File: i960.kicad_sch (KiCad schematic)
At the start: 49 parts

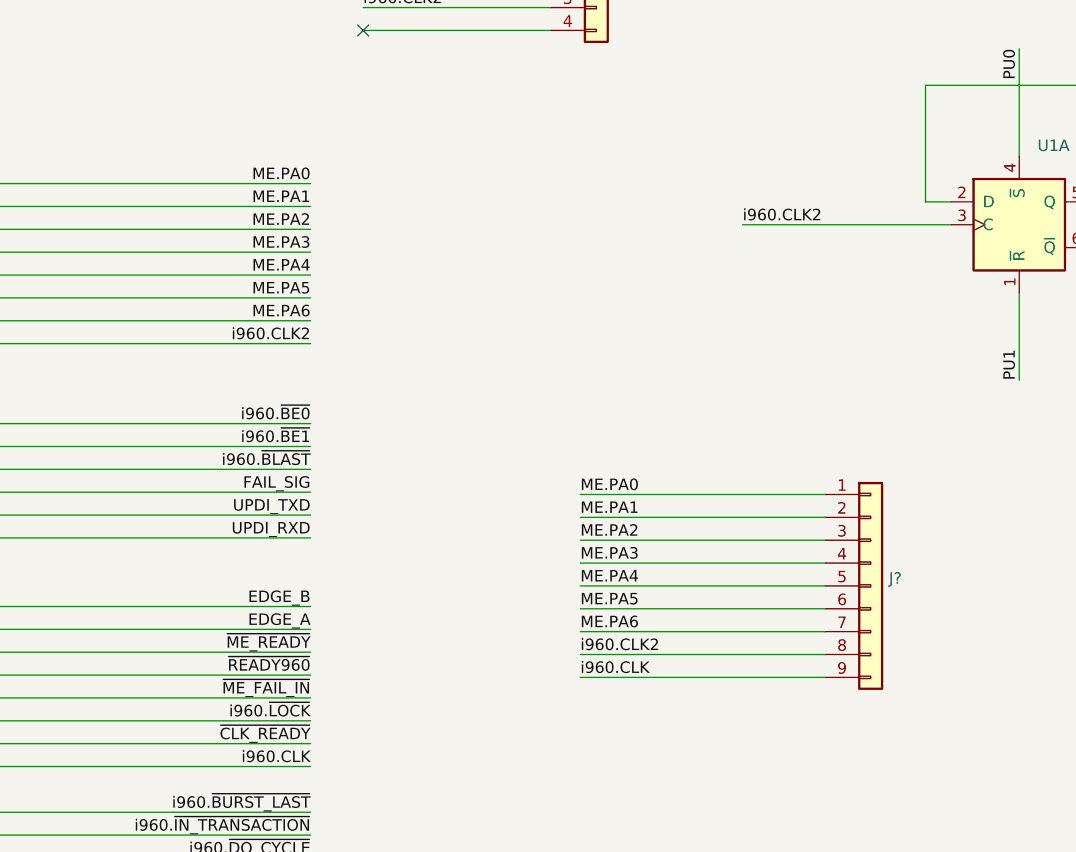
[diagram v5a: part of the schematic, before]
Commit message: Drop the HC125 and start redoing the pinout for the management engine to maximize layout capabilities
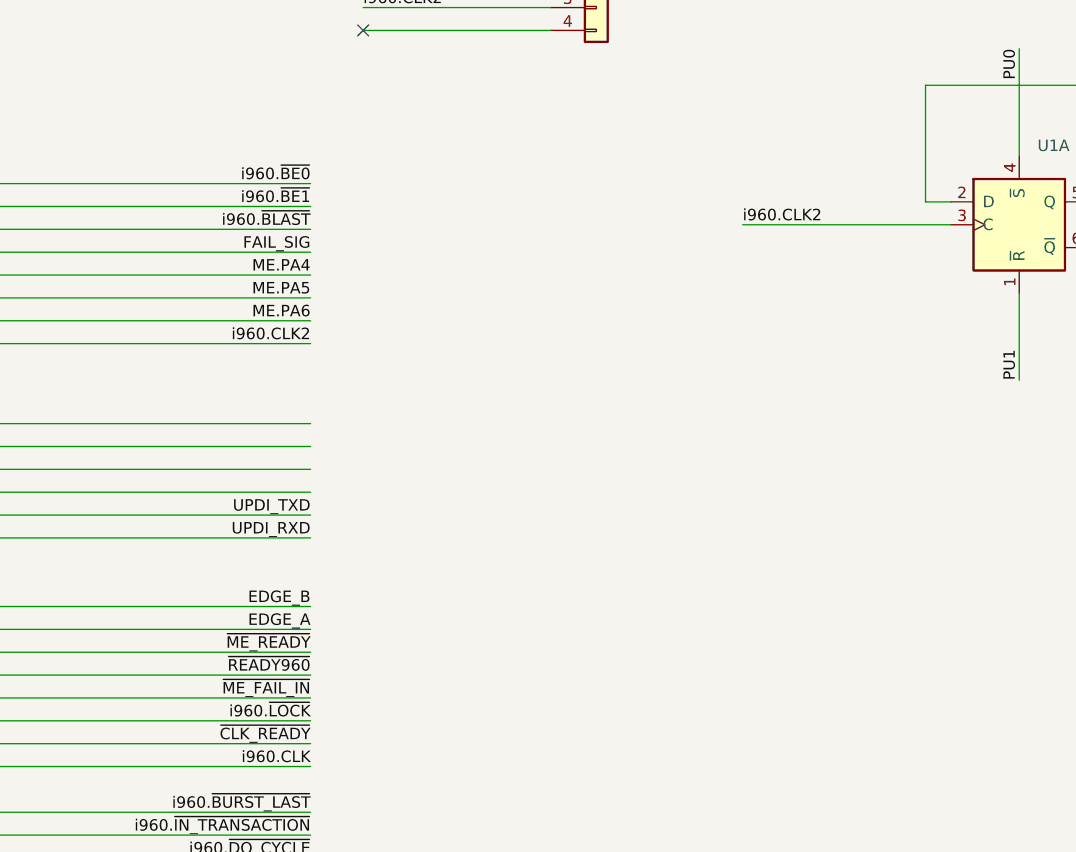
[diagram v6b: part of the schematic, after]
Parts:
- removed J?: (no value), symbol Connector_Generic:Conn_01x09
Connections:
- net ME.PA0 is gone; now on net i960.~{BE0}: U16.33 ((CLKI/TXD0/CCL0-IN0)PA0)
- net ME.PA1 is gone; now on net i960.~{BE1}: U16.34 ((RXD0/CCL0-IN1)PA1)
- net ME.PA2 is gone; now on net i960.~{BLAST}: U16.35 ((XCK0/SDA/CCL0-IN2)PA2)
- net ME.PA3 is gone; now on net FAIL_SIG: U16.36 ((XDIR0/SCL/CCL0-OUT)PA3)
- net FAIL_SIG: no longer U16.4 ((XDIR1/~{SS}_ALT/CCL1-OUT)PC3)
- net i960.~{BE0}: no longer U16.1 ((TXD1/MOSI_ALT/CCL1-IN0)PC0)
- net i960.~{BE1}: no longer U16.2 ((RXD1/MISO_ALT/CCL1-IN1)PC1)
- net i960.~{BLAST}: no longer U16.3 ((XCK1/SCK_ALT/CCL1-IN2)PC2)
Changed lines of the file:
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@@
-    (stroke (width 0) (type default) (color 0 0 0 0))
-  )
-  (wire (pts (xy 172.466 84.582) (xy 199.644 84.582))
     (stroke (width 0) (type default) (color 0 0 0 0))
   )
@@
     (stroke (width 0) (type default) (color 0 0 0 0))
   )
-  (wire (pts (xy 172.466 76.962) (xy 199.644 76.962))
-    (stroke (width 0) (type default) (color 0 0 0 0))
-  )
   (wire (pts (xy 514.604 80.264) (xy 542.29 80.264))
     (stroke (width 0) (type default) (color 0 0 0 0))
@@
     (stroke (width 0) (type default) (color 0 0 0 0))
   )
-  (wire (pts (xy 172.466 89.662) (xy 199.644 89.662))
-    (stroke (width 0) (type default) (color 0 0 0 0))
-  )
   (wire (pts (xy 45.212 135.128) (xy 45.212 118.11))
     (stroke (width 0) (type default) (color 0 0 0 0))
@@
     (stroke (width 0) (type default) (color 0 0 0 0))
   )
-  (wire (pts (xy 172.466 79.502) (xy 199.644 79.502))
-    (stroke (width 0) (type default) (color 0 0 0 0))
-  )
   (wire (pts (xy 210.312 462.788) (xy 210.312 427.736))
     (stroke (width 0) (type default) (color 0 0 0 0))
@@
     (stroke (width 0) (type default) (color 0 0 0 0))
   )
-  (wire (pts (xy 172.466 97.282) (xy 199.644 97.282))
-    (stroke (width 0) (type default) (color 0 0 0 0))
-  )
   (wire (pts (xy 59.69 61.468) (xy 20.066 61.468))
     (stroke (width 0) (type default) (color 0 0 0 0))
@@
     (stroke (width 0) (type default) (color 0 0 0 0))
   )
-  (wire (pts (xy 172.466 82.042) (xy 199.644 82.042))
-    (stroke (width 0) (type default) (color 0 0 0 0))
-  )
   (wire (pts (xy 23.876 364.236) (xy 54.102 364.236))
     (stroke (width 0) (type default) (color 0 0 0 0))
@@
     (stroke (width 0) (type default) (color 0 0 0 0))
   )
-  (wire (pts (xy 172.466 94.742) (xy 199.644 94.742))
-    (stroke (width 0) (type default) (color 0 0 0 0))
-  )
   (wire (pts (xy 467.106 57.404) (xy 502.92 57.404))
     (stroke (width 0) (type default) (color 0 0 0 0))
@@
     (stroke (width 0) (type default) (color 0 0 0 0))
   )
-  (wire (pts (xy 172.466 92.202) (xy 199.644 92.202))
-    (stroke (width 0) (type default) (color 0 0 0 0))
-  )
   (wire (pts (xy 346.71 266.446) (xy 377.698 266.446))
     (stroke (width 0) (type default) (color 0 0 0 0))
@@
   )
   (wire (pts (xy 148.336 25.4) (xy 169.164 25.4))
-    (stroke (width 0) (type default) (color 0 0 0 0))
-  )
-  (wire (pts (xy 172.466 87.122) (xy 199.644 87.122))
     (stroke (width 0) (type default) (color 0 0 0 0))
   )
@@
     (effects (font (size 1.27 1.27)) (justify left bottom))
   )
-  (label "FAIL_SIG" (at 142.494 76.708 180)
+  (label "FAIL_SIG" (at 142.494 50.038 180)
     (effects (font (size 1.27 1.27)) (justify right bottom))
   )
@@
     (effects (font (size 1.27 1.27)) (justify left bottom))
   )
-  (label "ME.PA4" (at 172.466 87.122 0)
-    (effects (font (size 1.27 1.27)) (justify left bottom))
-  )
   (label "~{RESET_INTERMEDIATE}" (at 142.494 132.588 180)
     (effects (font (size 1.27 1.27)) (justify right bottom))
@@
     (effects (font (size 1.27 1.27)) (justify right bottom))
   )
-  (label "ME.PA0" (at 172.466 76.962 0)
-    (effects (font (size 1.27 1.27)) (justify left bottom))
-  )
   (label "AD1" (at 405.892 44.704 0)
     (effects (font (size 1.27 1.27)) (justify left bottom))
@@
     (effects (font (size 1.27 1.27)) (justify left bottom))
   )
-  (label "ME.PA1" (at 172.466 79.502 0)
-    (effects (font (size 1.27 1.27)) (justify left bottom))
-  )
   (label "i960.D0" (at 489.966 170.942 0)
     (effects (font (size 1.27 1.27)) (justify left bottom))
@@
     (effects (font (size 1.27 1.27)) (justify left bottom))
   )
-  (label "i960.CLK2" (at 172.466 94.742 0)
-    (effects (font (size 1.27 1.27)) (justify left bottom))
-  )
   (label "PU3" (at 294.386 119.634 90)
     (effects (font (size 1.27 1.27)) (justify left bottom))
@@
     (effects (font (size 1.27 1.27)) (justify right bottom))
   )
-  (label "ME.PA2" (at 142.494 47.498 180)
-    (effects (font (size 1.27 1.27)) (justify right bottom))
-  )
   (label "PU0" (at 221.234 27.432 270)
     (effects (font (size 1.27 1.27)) (justify right bottom))
@@
     (effects (font (size 1.27 1.27)) (justify right bottom))
   )
-  (label "i960.~{BLAST}" (at 142.494 74.168 180)
+  (label "i960.~{BLAST}" (at 142.494 47.498 180)
     (effects (font (size 1.27 1.27)) (justify right bottom))
   )
@@
     (effects (font (size 1.27 1.27)) (justify right bottom))
   )
-  (label "ME.PA5" (at 172.466 89.662 0)
-    (effects (font (size 1.27 1.27)) (justify left bottom))
-  )
   (label "AD6" (at 405.892 57.404 0)
     (effects (font (size 1.27 1.27)) (justify left bottom))
@@
     (effects (font (size 1.27 1.27)) (justify left bottom))
   )
-  (label "ME.PA1" (at 142.494 44.958 180)
-    (effects (font (size 1.27 1.27)) (justify right bottom))
-  )
   (label "GCM4.L7" (at 477.52 191.516 180)
     (effects (font (size 1.27 1.27)) (justify right bottom))
@@
     (effects (font (size 1.27 1.27)) (justify left bottom))
   )
-  (label "ME.PA3" (at 142.494 50.038 180)
-    (effects (font (size 1.27 1.27)) (justify right bottom))
-  )
-  (label "i960.~{BE0}" (at 142.494 69.088 180)
+  (label "i960.~{BE0}" (at 142.494 42.418 180)
     (effects (font (size 1.27 1.27)) (justify right bottom))
   )
@@
     (effects (font (size 1.27 1.27)) (justify left bottom))
   )
-  (label "i960.~{BE1}" (at 142.494 71.628 180)
-    (effects (font (size 1.27 1.27)) (justify right bottom))
-  )
-  (label "ME.PA3" (at 172.466 84.582 0)
-    (effects (font (size 1.27 1.27)) (justify left bottom))
+  (label "i960.~{BE1}" (at 142.494 44.958 180)
+    (effects (font (size 1.27 1.27)) (justify right bottom))
   )
   (label "i960.A21" (at 515.874 72.644 0)
@@
     (effects (font (size 1.27 1.27)) (justify right bottom))
   )
-  (label "ME.PA2" (at 172.466 82.042 0)
-    (effects (font (size 1.27 1.27)) (justify left bottom))
-  )
   (label "i960.CLK2" (at 514.604 28.448 0)
     (effects (font (size 1.27 1.27)) (justify left bottom))
@@
     (effects (font (size 1.27 1.27)) (justify left bottom))
   )
-  (label "ME.PA0" (at 142.494 42.418 180)
-    (effects (font (size 1.27 1.27)) (justify right bottom))
-  )
   (label "i960.~{BURST_LAST}" (at 190.754 439.928 0)
     (effects (font (size 1.27 1.27)) (justify left bottom))
@@
     (effects (font (size 1.27 1.27)) (justify right bottom))
   )
-  (label "i960.CLK" (at 172.466 97.282 0)
-    (effects (font (size 1.27 1.27)) (justify left bottom))
-  )
   (label "i960.~{AS}" (at 570.738 173.482 180)
     (effects (font (size 1.27 1.27)) (justify right bottom))
@@
   )
   (label "i960.~{INT0}" (at 450.342 393.954 0)
-    (effects (font (size 1.27 1.27)) (justify left bottom))
-  )
-  (label "ME.PA6" (at 172.466 92.202 0)
     (effects (font (size 1.27 1.27)) (justify left bottom))
   )
@@
     (pin "1")
   )
-  (symbol (lib_id "Connector_Generic:Conn_01x09") (at 204.724 87.122 0) (unit 1)
-    (in_bom yes) (on_board yes) (fields_autoplaced)
-    (property "Reference" "J?" (id 0) (at 206.756 86.2873 0)
-      (effects (font (size 1.27 1.27)) (justify left))
-    )
-    (property "Value" "" (id 1) (at 206.756 88.8242 0)
-      (effects (font (size 1.27 1.27)) (justify left))
-    )
-    (property "Footprint" "" (id 2) (at 204.724 87.122 0)
-      (effects (font (size 1.27 1.27)) hide)
-    )
-    (property "Datasheet" "~" (id 3) (at 204.724 87.122 0)
-      (effects (font (size 1.27 1.27)) hide)
-    )
-    (pin "1")
-    (pin "2")
-    (pin "3")
-    (pin "4")
-    (pin "5")
-    (pin "6")
-    (pin "7")
-    (pin "8")
-    (pin "9")
-  )
   (symbol (lib_id "power:GND") (at 260.096 182.118 0) (unit 1)

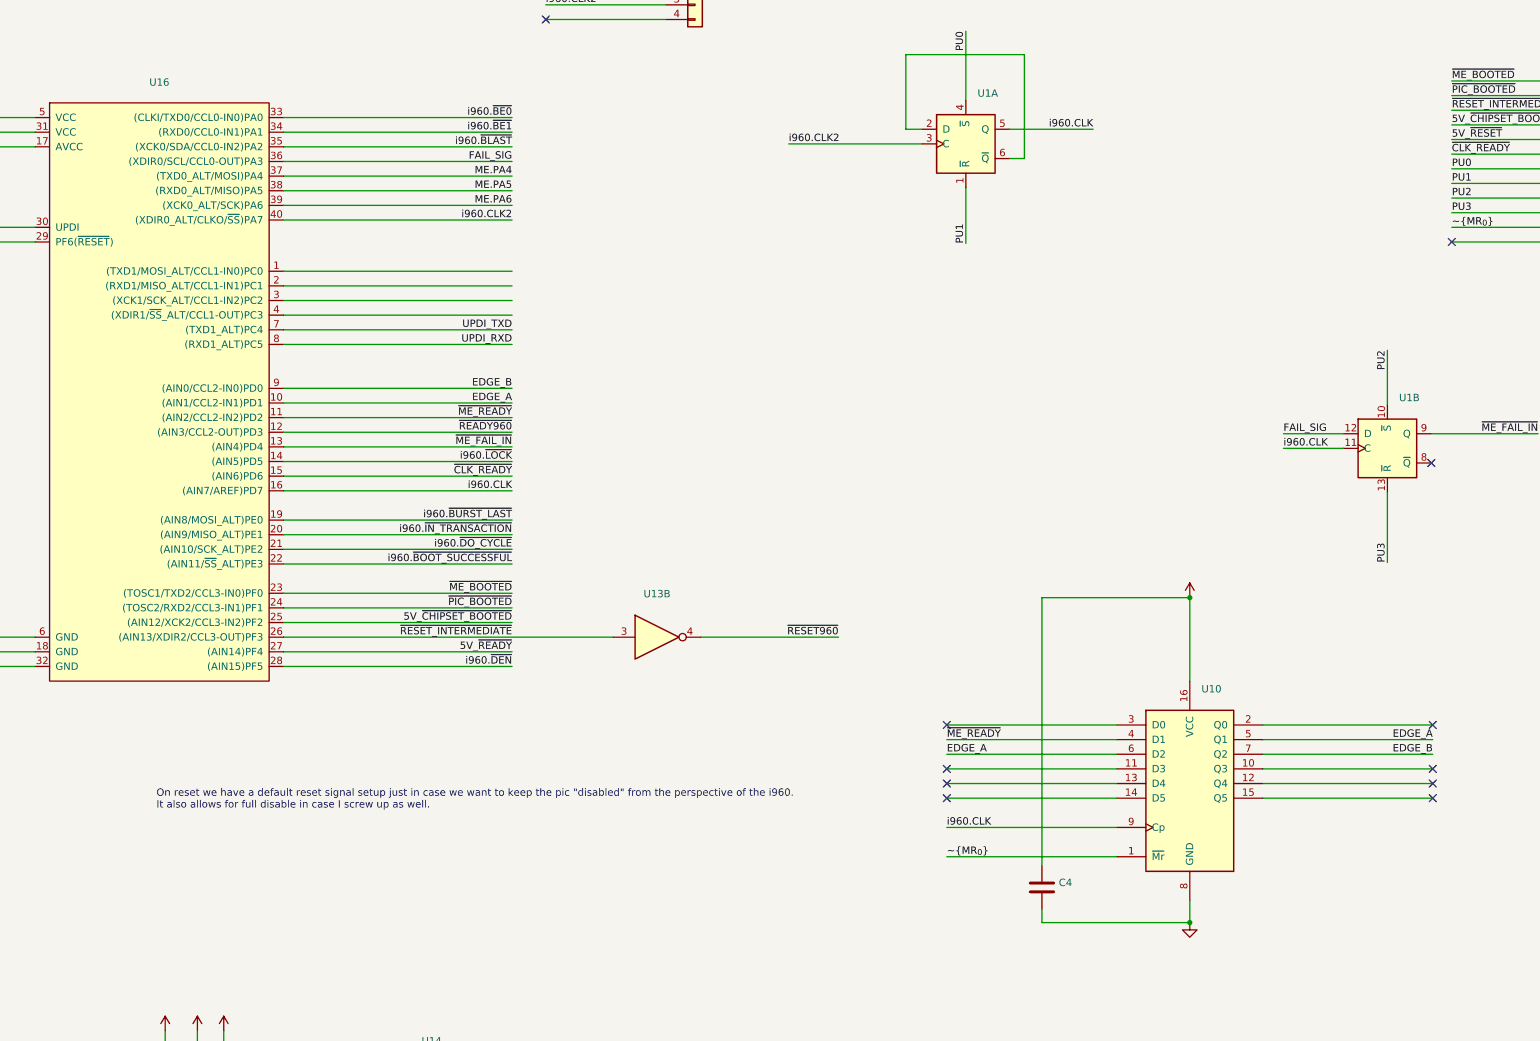
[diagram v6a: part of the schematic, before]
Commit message: Drop the 74AHC174 because the edge detector is fine.
Also don't use a CCL for the reset detection. Instead, the two CCLs are
way more useful for generating the 10mhz signal cleanly.

I also am going do the reset circuit manually because it makes way more
sense that way. I am even going to use the builtin pullups as well!

I can also get rid of the ME_BOOTED pin. Still need to do that
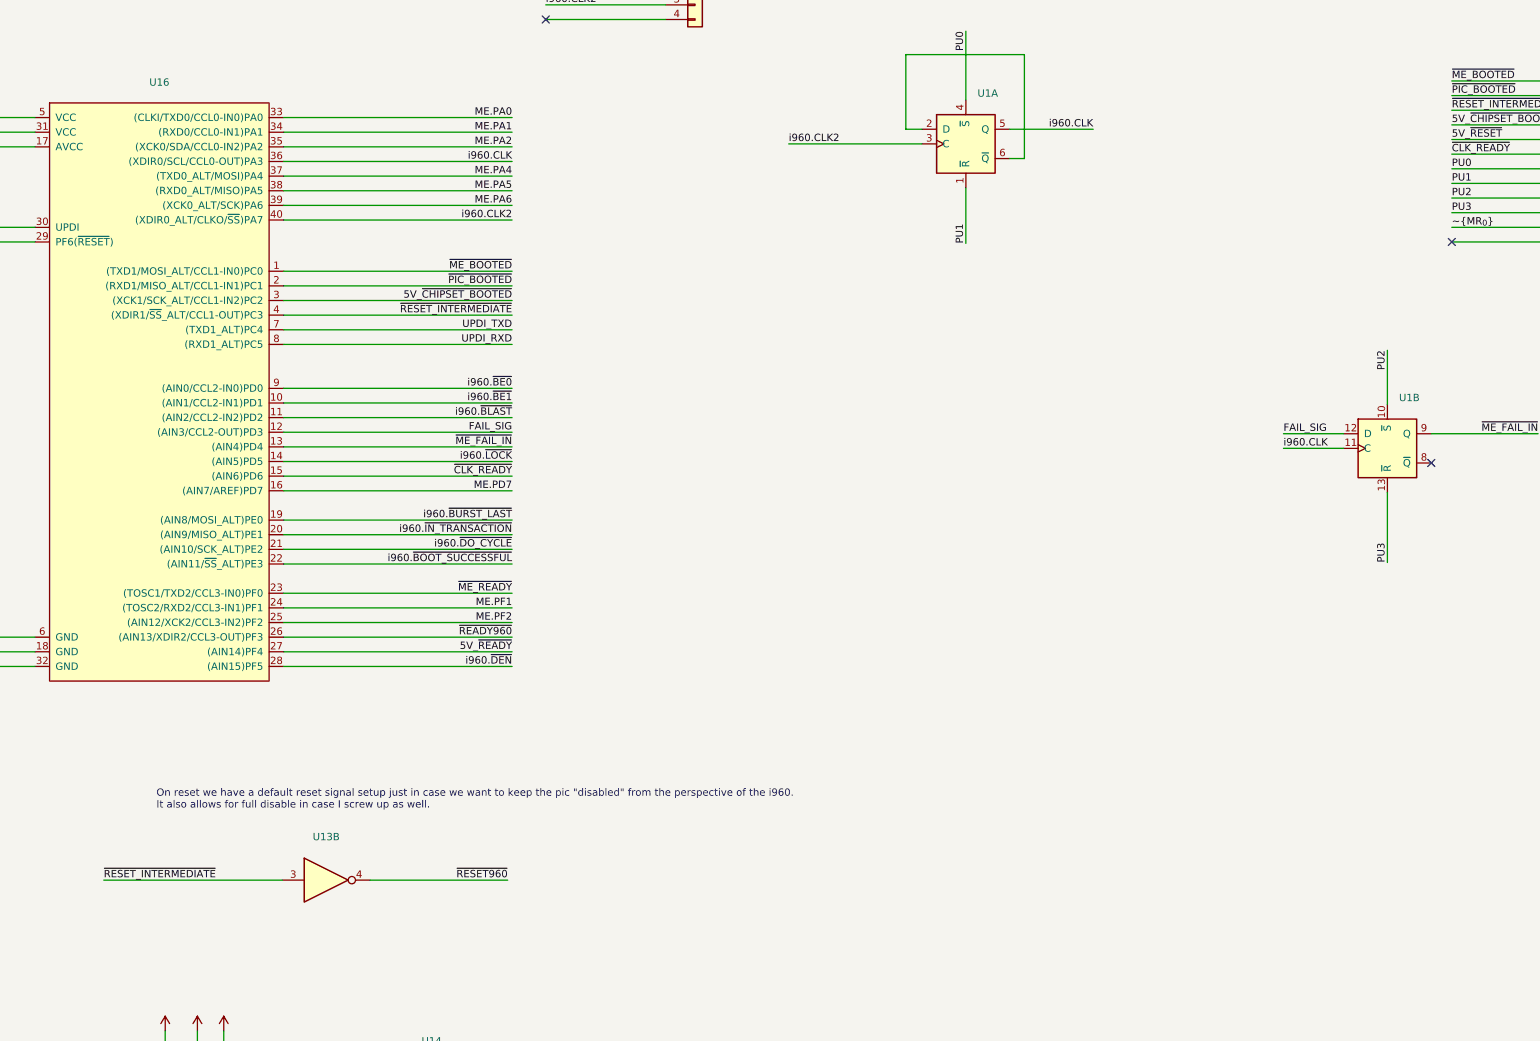
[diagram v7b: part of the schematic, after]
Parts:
- removed C4: (no value), symbol Device:C
- removed U10: (no value), symbol 74xx:74LS174
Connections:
- net EDGE_A is gone; now on net i960.~{BE1}: U16.10 ((AIN1/CCL2-IN1)PD1)
- net EDGE_B is gone; now on net i960.~{BE0}: U16.9 ((AIN0/CCL2-IN0)PD0)
- net 5V_~{CHIPSET_BOOTED}: now also U16.3 ((XCK1/SCK_ALT/CCL1-IN2)PC2); no longer U16.25 ((AIN12/XCK2/CCL3-IN2)PF2)
- net FAIL_SIG: now also U16.12 ((AIN3/CCL2-OUT)PD3); no longer U16.36 ((XDIR0/SCL/CCL0-OUT)PA3)
- net i960.CLK: now also U16.36 ((XDIR0/SCL/CCL0-OUT)PA3); no longer U16.16 ((AIN7/AREF)PD7)
- net i960.~{BE0}: no longer U16.33 ((CLKI/TXD0/CCL0-IN0)PA0)
- net i960.~{BE1}: no longer U16.34 ((RXD0/CCL0-IN1)PA1)
- net i960.~{BLAST}: now also U16.11 ((AIN2/CCL2-IN2)PD2); no longer U16.35 ((XCK0/SDA/CCL0-IN2)PA2)
- net ~{ME_BOOTED}: now also U16.1 ((TXD1/MOSI_ALT/CCL1-IN0)PC0); no longer U16.23 ((TOSC1/TXD2/CCL3-IN0)PF0)
- net ~{ME_READY}: now also U16.23 ((TOSC1/TXD2/CCL3-IN0)PF0); no longer U16.11 ((AIN2/CCL2-IN2)PD2)
- net ~{PIC_BOOTED}: now also U16.2 ((RXD1/MISO_ALT/CCL1-IN1)PC1); no longer U16.24 ((TOSC2/RXD2/CCL3-IN1)PF1)
- net ~{READY960}: now also U16.26 ((AIN13/XDIR2/CCL3-OUT)PF3); no longer U16.12 ((AIN3/CCL2-OUT)PD3)
- net ~{RESET_INTERMEDIATE}: now also U16.4 ((XDIR1/~{SS}_ALT/CCL1-OUT)PC3); no longer U16.26 ((AIN13/XDIR2/CCL3-OUT)PF3)
- new net ME.PA0: U16.33 ((CLKI/TXD0/CCL0-IN0)PA0)
- new net ME.PA1: U16.34 ((RXD0/CCL0-IN1)PA1)
- new net ME.PA2: U16.35 ((XCK0/SDA/CCL0-IN2)PA2)
- new net ME.PD7: U16.16 ((AIN7/AREF)PD7)
- new net ME.PF1: U16.24 ((TOSC2/RXD2/CCL3-IN1)PF1)
- new net ME.PF2: U16.25 ((AIN12/XCK2/CCL3-IN2)PF2)
- no-connect marks 21 -> 13
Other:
- moved on the sheet: U13B
